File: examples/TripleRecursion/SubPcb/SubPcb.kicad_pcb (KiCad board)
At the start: 2 copper layers, 11.3 x 8.9 mm, 7 parts, among them J1 Screw_Terminal_01x04, Q1 MMBT2222A, Q2 BC807

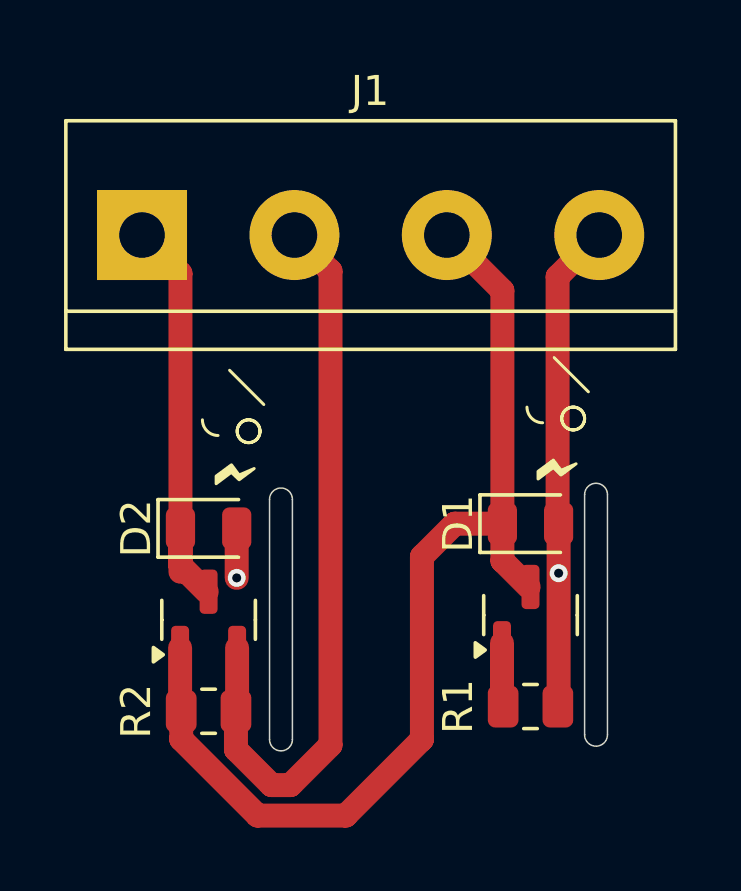
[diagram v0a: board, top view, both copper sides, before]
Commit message: Add Zones to Examples
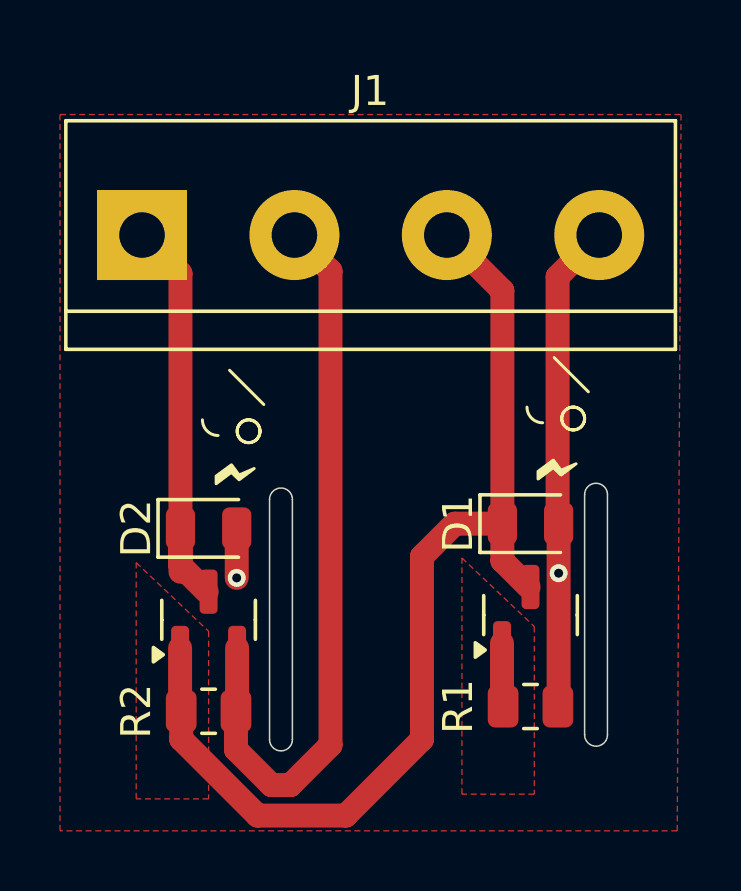
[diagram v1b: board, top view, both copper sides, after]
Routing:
- added copper zone on F.Cu, net /Input
- added copper zone on F.Cu, net /nType/Output
- added copper zone on F.Cu, net GND
